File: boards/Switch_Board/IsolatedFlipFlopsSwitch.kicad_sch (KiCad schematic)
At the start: 11 parts, among them IC1 ISO6520FDR, U16 PTPS22811LRPWR, U3 74AUP1G79

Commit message: footprints added
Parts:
- IC1: footprint SOIC127P600X175-8N -> Package_SO:SOIC-8_3.9x4.9mm_P1.27mm
- U16: footprint VQFN10_RPW_TEX -> Package_VQFN:VQFN-HR-RPW0010A
- U3: footprint (none) -> Package_TO_SOT_SMD:SOT-23-5
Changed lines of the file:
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@@
 			)
 		)
-		(property "Footprint" "VQFN10_RPW_TEX"
+		(property "Footprint" "Package_VQFN:VQFN-HR-RPW0010A"
 			(at 196.85 87.63 0)
 			(effects
@@
 			)
 		)
-		(property "Footprint" ""
+		(property "Footprint" "Package_TO_SOT_SMD:SOT-23-5"
 			(at 133.35 96.52 0)
 			(effects
@@
 			)
 		)
-		(property "Footprint" "SOIC127P600X175-8N"
+		(property "Footprint" "Package_SO:SOIC-8_3.9x4.9mm_P1.27mm"
 			(at 99.06 187.63 0)
 			(effects

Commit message: updated schematic and pcb
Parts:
- added J1: Screw_Terminal_01x02, Resistor_THT:R_Axial_DIN0204_L3.6mm_D1.6mm_P5.08mm_Horizontal, symbol Connector:Screw_Terminal_01x02
- 500k8, R29, R30, R31, R32: footprint (none) -> Resistor_SMD:R_0603_1608Metric
- BT3: footprint (none) -> TerminalBlock:TerminalBlock_MaiXu_MX126-5.0-02P_1x02_P5.00mm
- C8: footprint (none) -> Capacitor_SMD:C_0603_1608Metric
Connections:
- net SubBatt_GND_1: now also J1.2 (Pin_2)
- net Switch_V_1: no longer names the net of C8.1, R32.1, U16.6 (OUT)
- net Switch_V_1: now also J1.1 (Pin_1)
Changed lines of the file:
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@@
+	)
+	(junction
+		(at 259.08 113.03)
+		(diameter 0)
+		(color 0 0 0 0)
 	)
 	(junction
@@
 	(wire
 		(pts
+			(xy 269.24 81.28) (xy 269.24 113.03)
+		)
+		(stroke
+			(width 0)
+			(type default)
+		)
+	)
+	(wire
+		(pts
 			(xy 187.96 92.71) (xy 201.93 92.71)
 		)
@@
 	(wire
 		(pts
-			(xy 259.08 78.74) (xy 264.16 78.74)
+			(xy 259.08 78.74) (xy 269.24 78.74)
 		)
 		(stroke
@@
 		(pts
 			(xy 187.96 113.03) (xy 223.52 113.03)
+		)
+		(stroke
+			(width 0)
+			(type default)
+		)
+	)
+	(wire
+		(pts
+			(xy 269.24 113.03) (xy 259.08 113.03)
 		)
 		(stroke
@@
 			)
 			(justify right)
-		)
-	)
-	(hierarchical_label "Switch_V_1"
-		(shape output)
-		(at 264.16 78.74 0)
-		(effects
-			(font
-				(size 1.27 1.27)
-			)
-			(justify left)
 		)
 	)
@@
 			)
 		)
-		(property "Footprint" ""
+		(property "Footprint" "Resistor_SMD:R_0603_1608Metric"
 			(at 252.984 93.726 90)
 			(effects
@@
 			)
 		)
-		(property "Footprint" ""
+		(property "Footprint" "Capacitor_SMD:C_0603_1608Metric"
 			(at 260.0452 88.9 0)
 			(effects
@@
 			)
 		)
-		(property "Footprint" ""
+		(property "Footprint" "Resistor_SMD:R_0603_1608Metric"
 			(at 188.976 108.204 90)
 			(effects
@@
 			)
 		)
-		(property "Footprint" ""
+		(property "Footprint" "Resistor_SMD:R_0603_1608Metric"
 			(at 188.976 98.044 90)
 			(effects
@@
 			)
 		)
-		(property "Footprint" ""
+		(property "Footprint" "TerminalBlock:TerminalBlock_MaiXu_MX126-5.0-02P_1x02_P5.00mm"
 			(at 38.1 97.536 90)
 			(effects
@@
 			)
 		)
-		(property "Footprint" ""
+		(property "Footprint" "Resistor_SMD:R_0603_1608Metric"
 			(at 227.584 109.474 90)
 			(effects
@@
 				(path "/27fcebe4-2fb8-4847-92ca-f98a7b250261/c95baff8-5754-4c60-b8c7-1f7ffe4a1015"
 					(reference "R11")
+					(unit 1)
+				)
+			)
+		)
+	)
+	(symbol
+		(lib_id "Connector:Screw_Terminal_01x02")
+		(at 274.32 78.74 0)
+		(unit 1)
+		(exclude_from_sim no)
+		(in_bom yes)
+		(on_board yes)
+		(dnp no)
+		(fields_autoplaced yes)
+		(property "Reference" "J1"
+			(at 276.86 78.7399 0)
+			(effects
+				(font
+					(size 1.27 1.27)
+				)
+				(justify left)
+			)
+		)
+		(property "Value" "Screw_Terminal_01x02"
+			(at 276.86 81.2799 0)
+			(effects
+				(font
+					(size 1.27 1.27)
+				)
+				(justify left)
+			)
+		)
+		(property "Footprint" "Resistor_THT:R_Axial_DIN0204_L3.6mm_D1.6mm_P5.08mm_Horizontal"
+			(at 274.32 78.74 0)
+			(effects
+				(font
+					(size 1.27 1.27)
+				)
+				(hide yes)
+			)
+		)
+		(property "Datasheet" "~"
+			(at 274.32 78.74 0)
+			(effects
+				(font
+					(size 1.27 1.27)
+				)
+				(hide yes)
+			)
+		)
+		(property "Description" "Generic screw terminal, single row, 01x02, script generated (kicad-library-utils/schlib/autogen/connector/)"
+			(at 274.32 78.74 0)
+			(effects
+				(font
+					(size 1.27 1.27)
+				)
+				(hide yes)
+			)
+		)
+		(pin "2"
+		)
+		(pin "1"
+		)
+		(instances
+			(project "Switch_Board"
+				(path "/27fcebe4-2fb8-4847-92ca-f98a7b250261/0ac322e4-151b-4a9f-b39e-a207455d52d0"
+					(reference "J5")
+					(unit 1)
+				)
+				(path "/27fcebe4-2fb8-4847-92ca-f98a7b250261/22315eb0-74dc-4cbd-8bc5-2b5a239cef41"
+					(reference "J2")
+					(unit 1)
+				)
+				(path "/27fcebe4-2fb8-4847-92ca-f98a7b250261/7883bc24-035c-4803-95ad-0f695f6f0510"
+					(reference "J1")
+					(unit 1)
+				)
+				(path "/27fcebe4-2fb8-4847-92ca-f98a7b250261/9a8757b7-59d4-4710-8d66-ccd12e8d4244"
+					(reference "J3")
+					(unit 1)
+				)
+				(path "/27fcebe4-2fb8-4847-92ca-f98a7b250261/c1721fd8-e05c-4e88-a7d4-aa7e24310545"
+					(reference "J6")
+					(unit 1)
+				)
+				(path "/27fcebe4-2fb8-4847-92ca-f98a7b250261/c95baff8-5754-4c60-b8c7-1f7ffe4a1015"
+					(reference "J4")
 					(unit 1)
 				)
@@
 			)
 		)
-		(property "Footprint" ""
+		(property "Footprint" "Resistor_SMD:R_0603_1608Metric"
 			(at 247.396 86.614 90)
 			(effects

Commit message: updating schematic
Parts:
- removed J1: Screw_Terminal_01x02, Resistor_THT:R_Axial_DIN0204_L3.6mm_D1.6mm_P5.08mm_Horizontal, symbol Connector:Screw_Terminal_01x02
- added J8: Conn_01x02, symbol Connector_Generic:Conn_01x02
- renumbered 500k8 to 500k
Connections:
- net SubBatt_GND_1: now also J8.2 (Pin_2)
- net at C8.1, R32.1, U16.6 (OUT): now also J8.1 (Pin_1)
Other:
- moved on the sheet: 500k, BT3, C8, D8, IC1, R29, R30, R31, R32, U16, U3

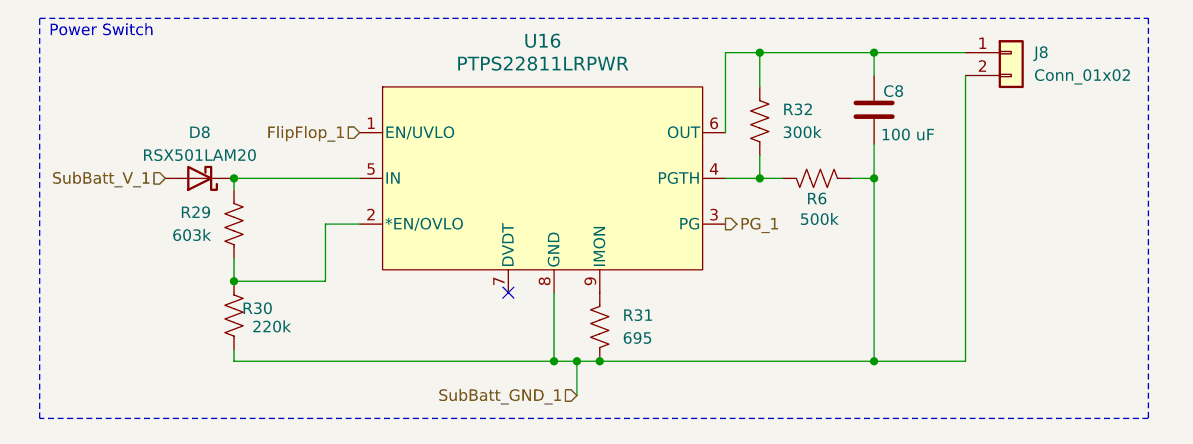
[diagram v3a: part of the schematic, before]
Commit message: status LEDs for switch
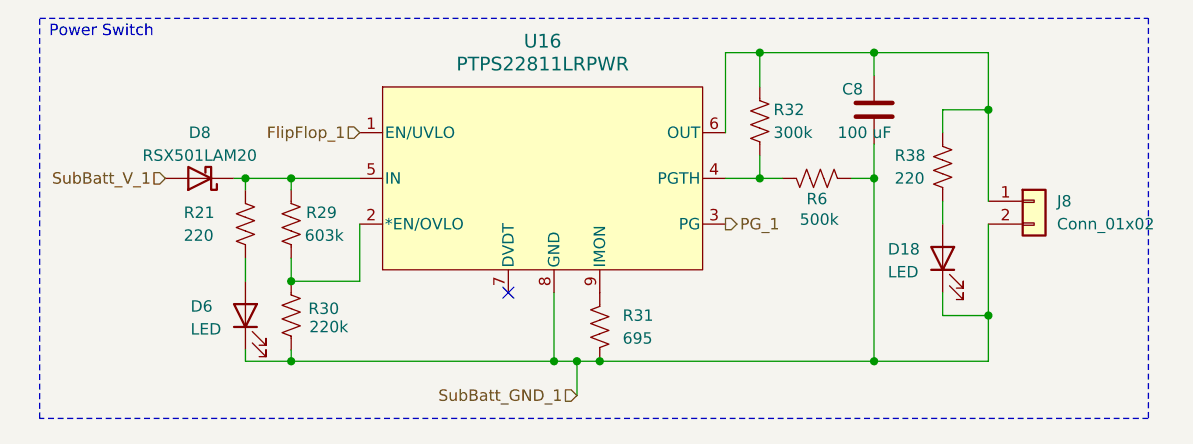
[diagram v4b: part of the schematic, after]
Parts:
- added D18, D6: LED, symbol Device:LED
- added R21, R38: 220, symbol Device:R_US
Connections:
- net SubBatt_GND_1: now also D18.1 (K), D6.1 (K)
- net at D8.1 (K), R29.1, U16.5 (IN): now also R21.1
- net at C8.1, J8.1 (Pin_1), R32.1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: now also R38.1
- new net: D18.2 (A), R38.2
- new net: D6.2 (A), R21.2
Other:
- moved on the sheet: J8, R29, R30

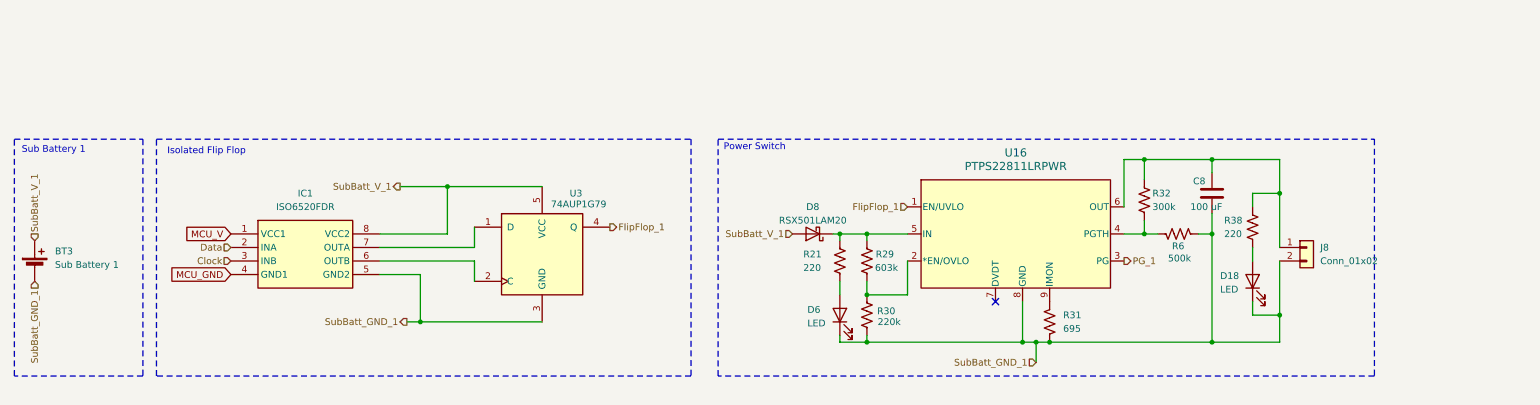
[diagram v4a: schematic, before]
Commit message: adding status LEDs, JST connectors, proper filter caps, and proof of concept for routing slice
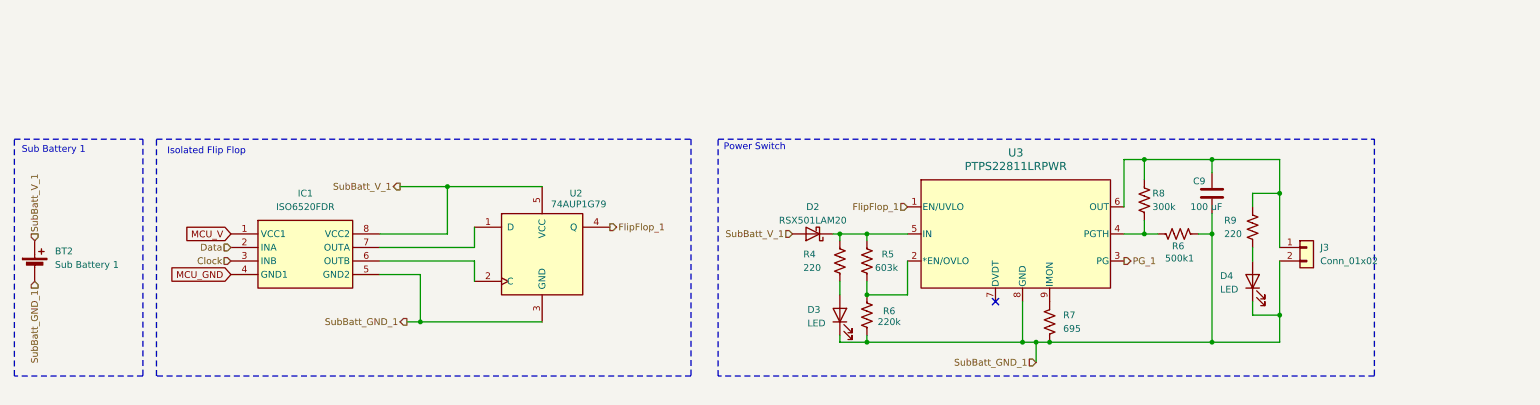
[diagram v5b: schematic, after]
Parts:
- BT2: renamed from BT3; footprint TerminalBlock:TerminalBlock_MaiXu_MX126-5.0-02P_1x02_P5.00mm -> Connector_JST:JST_PH_S2B-PH-SM4-TB_1x02-1MP_P2.00mm_Horizontal
- D3: renamed from D6; footprint (none) -> LED_SMD:LED_0603_1608Metric
- D4: renamed from D18; footprint (none) -> LED_SMD:LED_0603_1608Metric
- J3: renamed from J8; footprint (none) -> Connector_JST:JST_PH_S2B-PH-SM4-TB_1x02-1MP_P2.00mm_Horizontal
- R4: renamed from R21; footprint (none) -> Resistor_SMD:R_0603_1608Metric
- R9: renamed from R38; footprint (none) -> Resistor_SMD:R_0603_1608Metric
- U3: renamed from U16; footprint Package_VQFN:VQFN-HR-RPW0010A -> Package_DFN_QFN:Texas_RPU0010A_VQFN-HR-10_2x2mm_P0.5mm
- renumbered 500k to 500k1, C8 to C9, D8 to D2, R29 to R5, R30 to R6, R31 to R7, R32 to R8, U3 to U2

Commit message: regulator added for flip flops and isolator, also reverse polarity protection added for everything
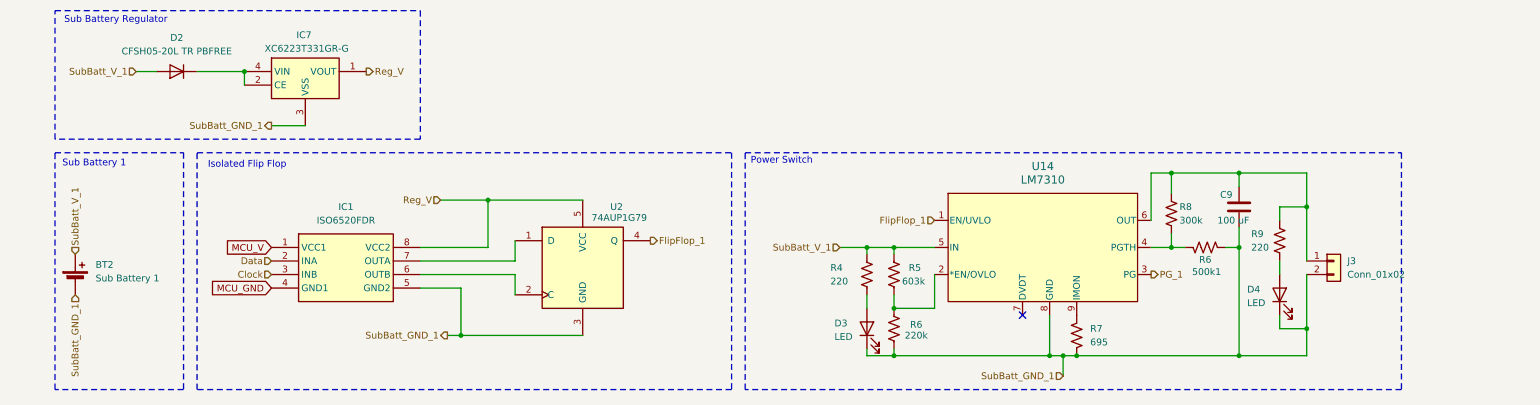
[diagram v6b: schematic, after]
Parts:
- removed D2: RSX501LAM20, Diode_SMD:D_SOD-128, symbol Device:D_Schottky
- removed U3: PTPS22811LRPWR, Package_DFN_QFN:Texas_RPU0010A_VQFN-HR-10_2x2mm_P0.5mm, symbol Switch_Texas:PTPS22811LRPWR
- added D2: CFSH05-20L TR PBFREE, Diode_ISS:CFSH0520LTRPBFREE, symbol Diode:1N4148WT
- added IC7: XC6223T331GR-G, SON60P160X120X60-5N, symbol Regulator_Torex:XC6223T331GR-G
- added U14: LM7310, Package_VQFN:VQFN-HR-RPW0010A, symbol Switch_Texas:LM7310
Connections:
- net FlipFlop_1: now also U14.1 (EN/UVLO)
- net PG_1: now also U14.3 (PG)
- net SubBatt_GND_1: now also IC7.3 (VSS), IC7.5 (EP), U14.8 (GND)
- net SubBatt_V_1: now also R4.1, R5.1, D2.2 (A), U14.5 (IN); no longer IC1.8 (VCC2), U2.5 (VCC)
- net at R5.2, R6.1: now also U14.2 (*EN/OVLO)
- net at 500k1.1, R8.2: now also U14.4 (PGTH)
- net at C9.1, J3.1 (Pin_1), R8.1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: now also U14.6 (OUT)
- net at R7.1: now also U14.9 (IMON)
- new net: D2.1 (K), IC7.2 (CE), IC7.4 (VIN)
- new net Reg_V: IC1.8 (VCC2), IC7.1 (VOUT), U2.5 (VCC)
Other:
- note added: "Sub Battery Regulator"
- moved on the sheet: 500k1, BT2, C9, D3, D4, IC1, J3, R4, R5, R6, R7, R8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

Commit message: Renaming a thing
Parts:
- BT2: value Sub Battery 1 -> Sub Battery
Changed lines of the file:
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@@
 			)
 		)
-		(property "Value" "Sub Battery 1"
+		(property "Value" "Sub Battery"
 			(at 33.02 104.8384 0)
 			(effects

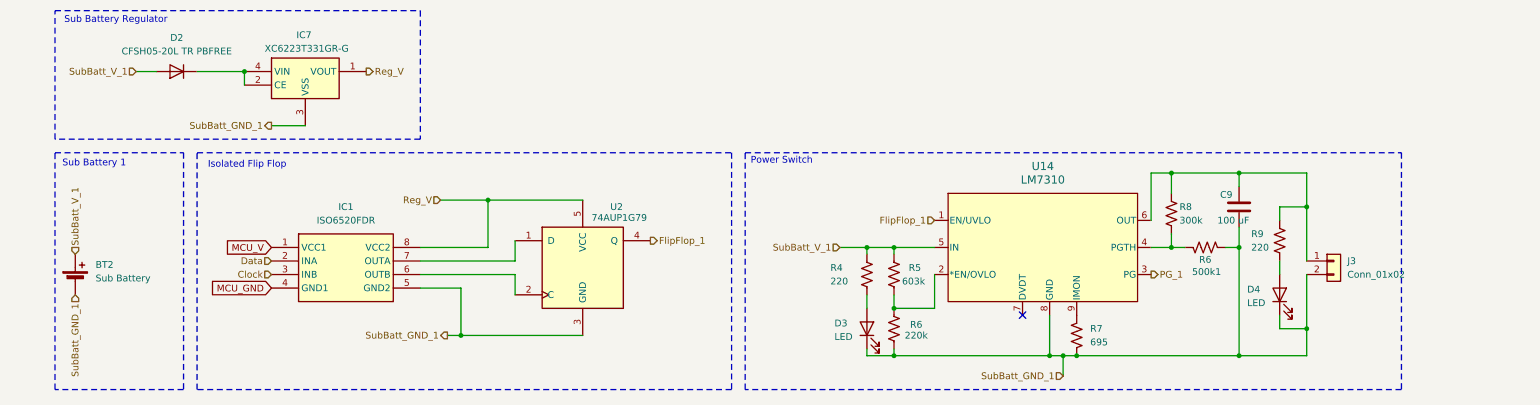
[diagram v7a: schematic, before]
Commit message: added caps to regulator and UART pins
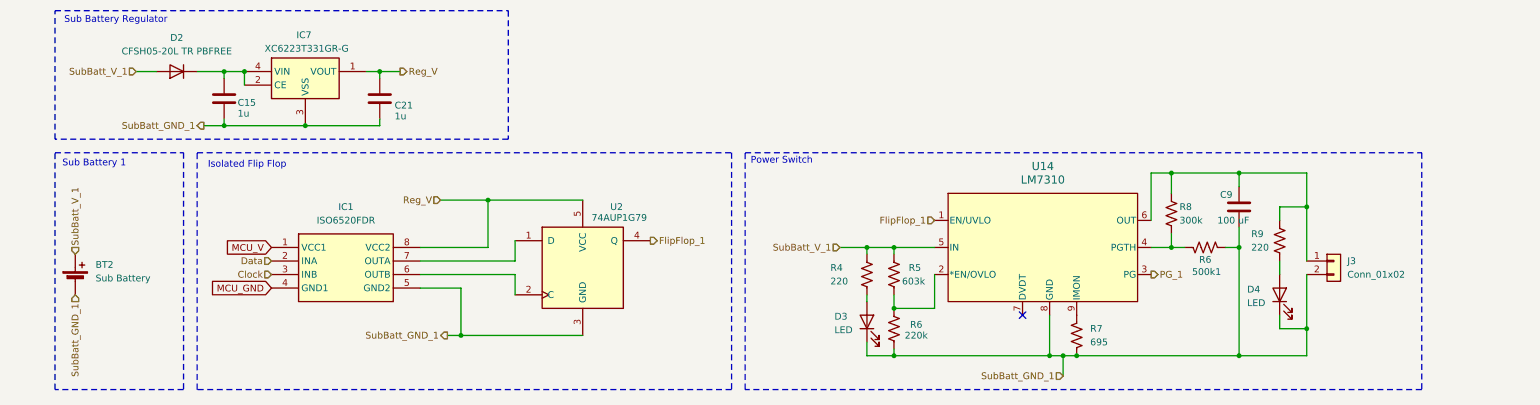
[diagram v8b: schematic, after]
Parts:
- added C15, C21: 1u, symbol Device:C
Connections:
- net Reg_V: now also C21.1
- net SubBatt_GND_1: now also C15.2, C21.2
- net at D2.1 (K), IC7.2 (CE), IC7.4 (VIN): now also C15.1
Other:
- moved on the sheet: D3
